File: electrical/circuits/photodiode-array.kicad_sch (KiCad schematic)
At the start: 19 parts, among them IC2 OPA695IDBVR, IC3 ADC08200CIMT_NOPB

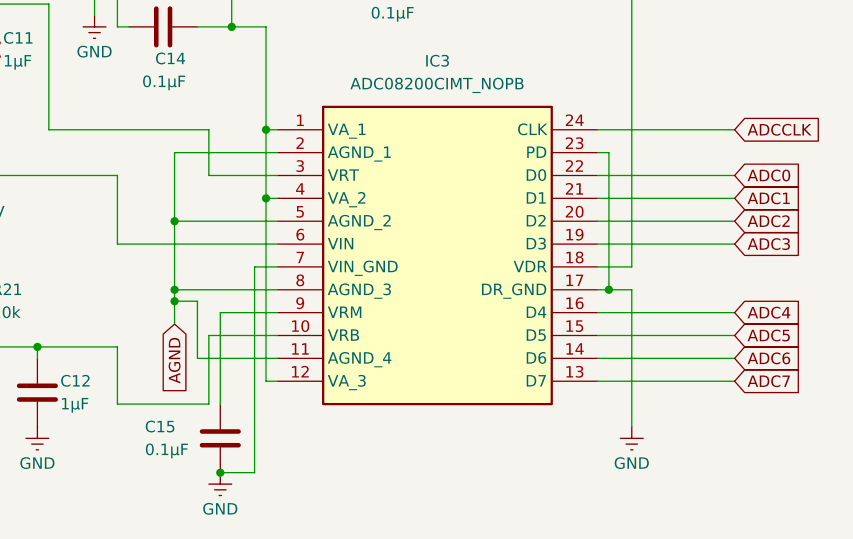
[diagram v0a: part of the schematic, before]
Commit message: Updated circuit schematics for 10BASE-T SNI mode
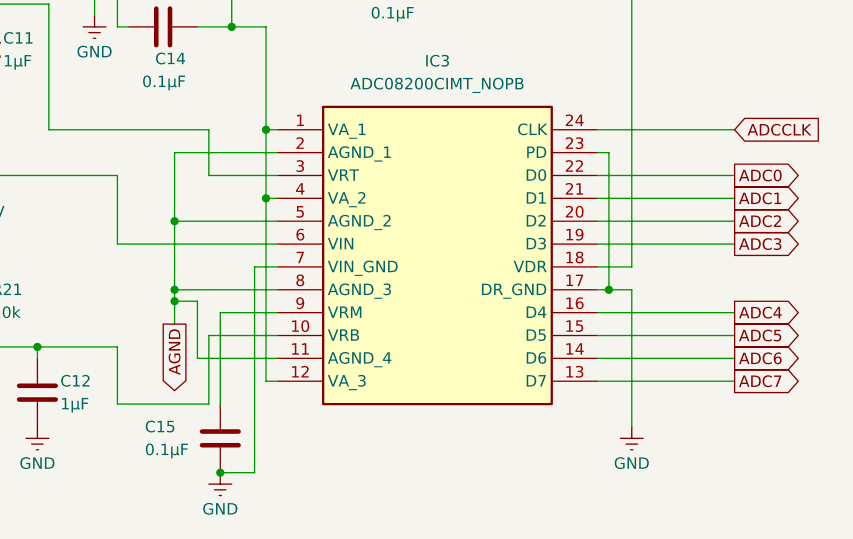
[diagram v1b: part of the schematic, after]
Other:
- title: (none) -> Free Space Optical 10BASE-T Ethernet Transceiver Circuit
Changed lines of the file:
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@@
 	(paper "A")
 	(title_block
-		(date "2025-07-15")
+		(title "Free Space Optical 10BASE-T Ethernet Transceiver Circuit")
+		(date "2025-07-22")
 	)
 	(junction
@@
 	)
 	(global_label "ADC0"
-		(shape input)
+		(shape output)
 		(at 203.2 95.25 0)
 		(fields_autoplaced yes)
@@
 	)
 	(global_label "ADC3"
-		(shape input)
+		(shape output)
 		(at 203.2 102.87 0)
 		(fields_autoplaced yes)
@@
 	)
 	(global_label "ADC5"
-		(shape input)
+		(shape output)
 		(at 203.2 113.03 0)
 		(fields_autoplaced yes)
@@
 	)
 	(global_label "ADC1"
-		(shape input)
+		(shape output)
 		(at 203.2 97.79 0)
 		(fields_autoplaced yes)
@@
 	)
 	(global_label "ADC7"
-		(shape input)
+		(shape output)
 		(at 203.2 118.11 0)
 		(fields_autoplaced yes)
@@
 	)
 	(global_label "ADC2"
-		(shape input)
+		(shape output)
 		(at 203.2 100.33 0)
 		(fields_autoplaced yes)
@@
 	)
 	(global_label "AGND"
-		(shape input)
+		(shape output)
 		(at 140.97 111.76 270)
 		(fields_autoplaced yes)
@@
 	)
 	(global_label "ADC4"
-		(shape input)
+		(shape output)
 		(at 203.2 110.49 0)
 		(fields_autoplaced yes)
@@
 	)
 	(global_label "ADC6"
-		(shape input)
+		(shape output)
 		(at 203.2 115.57 0)
 		(fields_autoplaced yes)
